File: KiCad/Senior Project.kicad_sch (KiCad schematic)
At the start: 32 parts, among them J1 USB_C_Receptacle_USB2.0_16P, J2 Screw_Terminal_01x02, J3 Screw_Terminal_01x06, SW1 SW_Push, SW2 SW_Push, U1 ESP32-S3FH4R2, X1 FC-135 32.7680KA-A5, Y2 Crystal_GND23

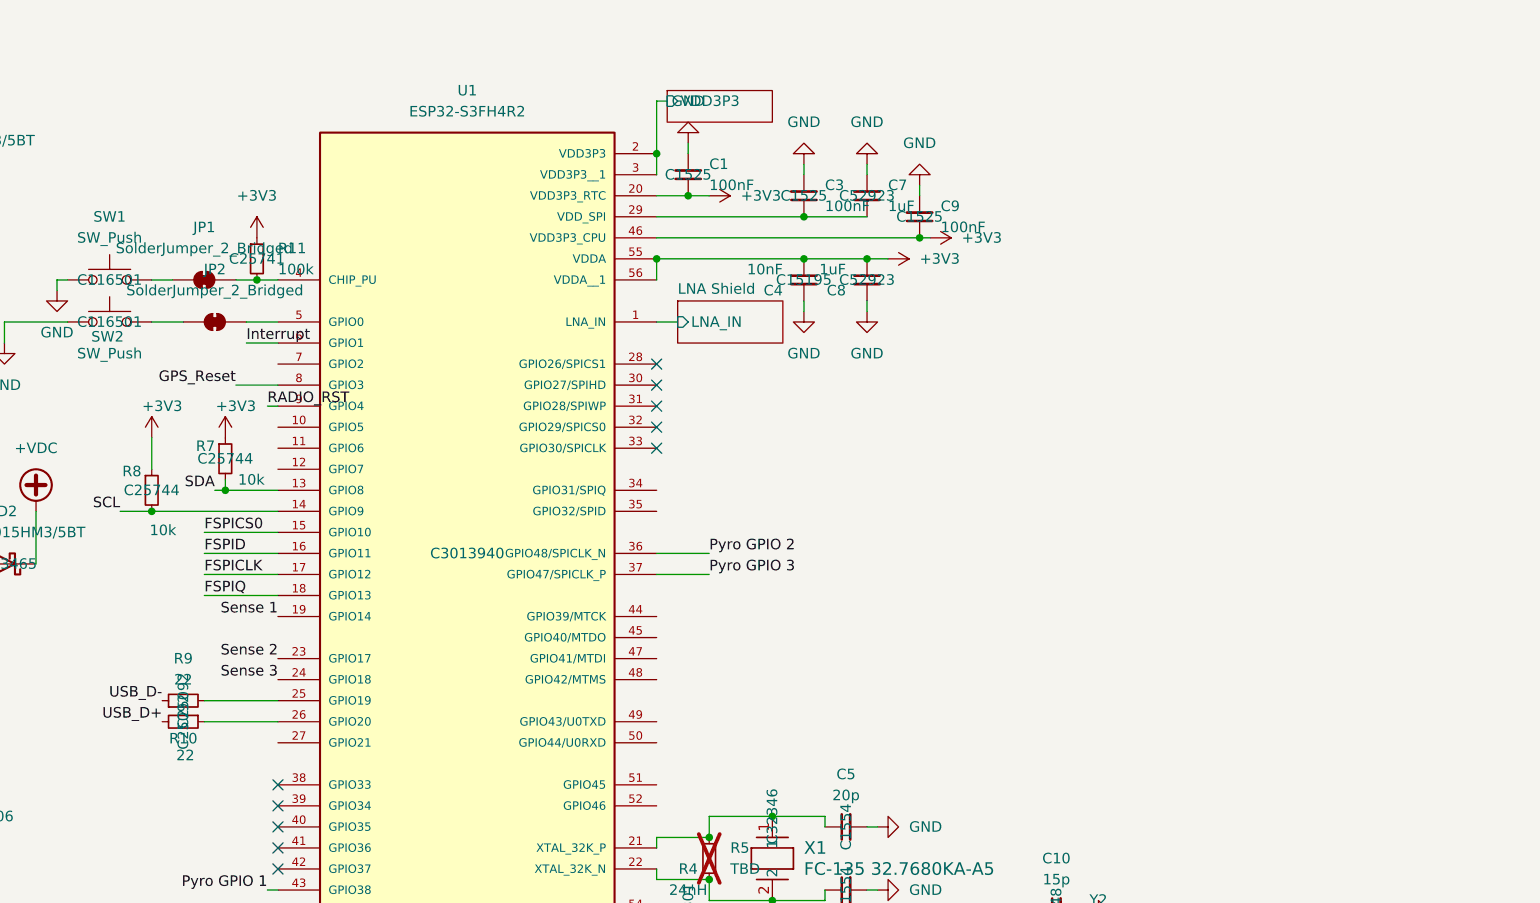
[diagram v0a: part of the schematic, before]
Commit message: adjustments to work with JLC and to match with example
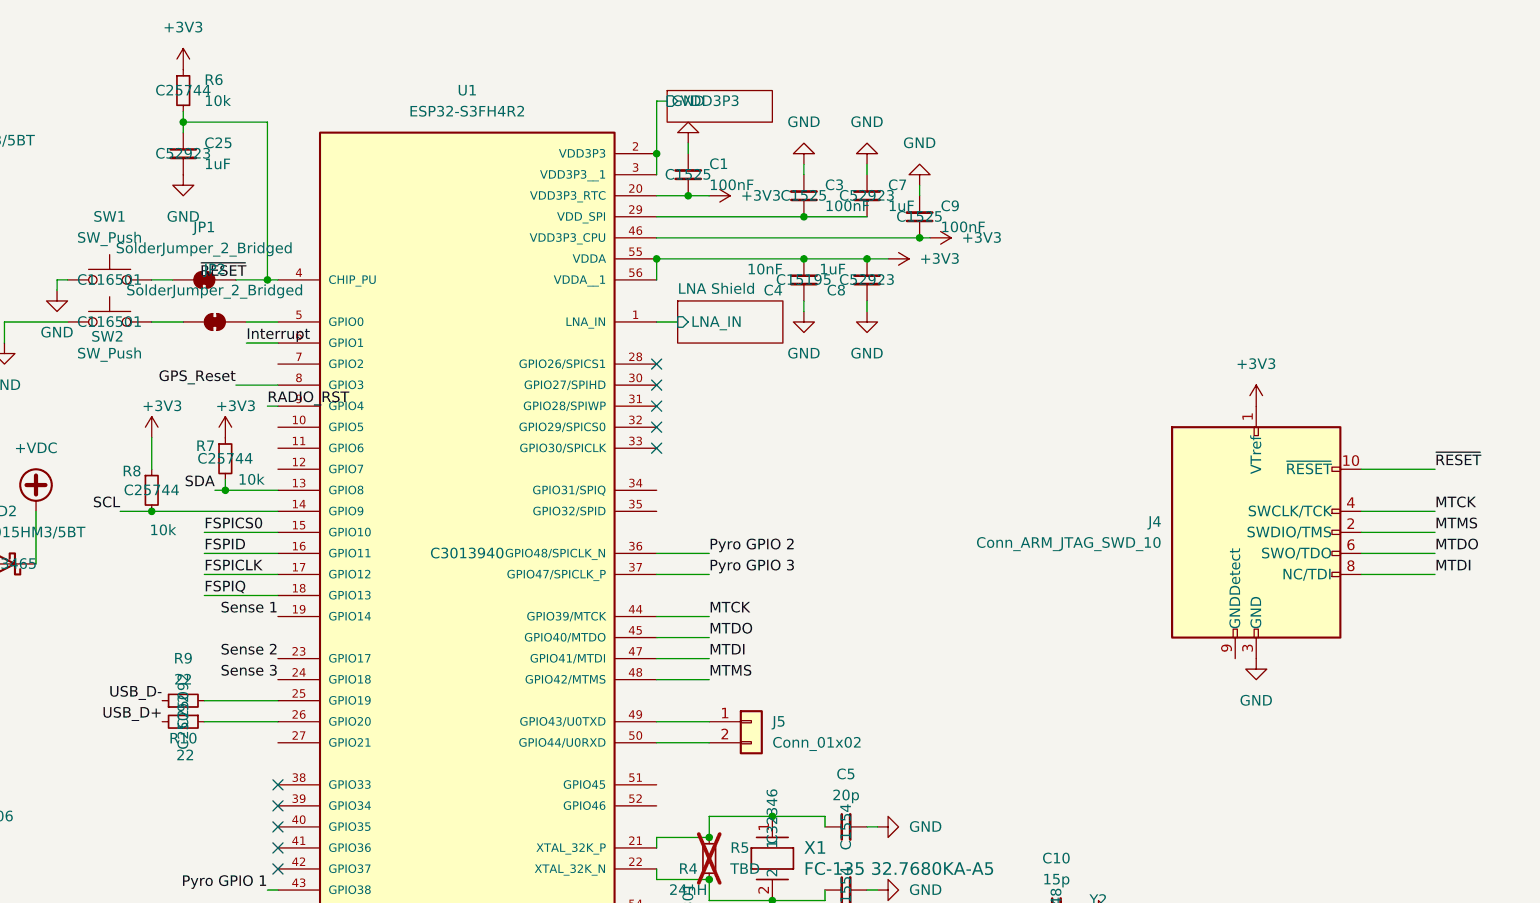
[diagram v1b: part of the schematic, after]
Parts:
- removed R11: 100k, Resistor_SMD:R_0402_1005Metric, symbol Device:R_Small
- added C25: 1uF, Capacitor_SMD:C_0402_1005Metric, symbol Device:C_Small
- added J4: Conn_ARM_JTAG_SWD_10, Connector_PinHeader_1.27mm:PinHeader_2x05_P1.27mm_Vertical_SMD, symbol Connector:Conn_ARM_JTAG_SWD_10
- added J5: Conn_01x02, Connector_PinHeader_1.27mm:PinHeader_1x02_P1.27mm_Vertical_SMD_Pin1Right, symbol Connector_Generic:Conn_01x02
- added R6: 10k, Resistor_SMD:R_0402_1005Metric, symbol Device:R_Small
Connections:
- net +3V3: now also J4.1 (VTref), R6.1
- net GND: now also C25.2, J4.3 (GND), J4.5 (GND)
- net ~{RESET}: now reaches JP1.2 (B), U1.4 (CHIP_PU)
- net ~{RESET}: now also C25.1, J4.10 (~{RESET}), R6.2
- net MTCK: now reaches U1.44 (GPIO39/MTCK)
- net MTCK: now also J4.4 (SWCLK/TCK)
- net MTDO: now reaches U1.45 (GPIO40/MTDO)
- net MTDO: now also J4.6 (SWO/TDO)
- net MTDI: now reaches U1.47 (GPIO41/MTDI)
- net MTDI: now also J4.8 (NC/TDI)
- net MTMS: now reaches U1.48 (GPIO42/MTMS)
- net MTMS: now also J4.2 (SWDIO/TMS)
- net at U1.49 (GPIO43/U0TXD): now also J5.1 (Pin_1)
- net at U1.50 (GPIO44/U0RXD): now also J5.2 (Pin_2)

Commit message: prepare to move barometer to front
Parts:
- J2, J3, J4, J5: now not fitted
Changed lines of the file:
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@@
 		(in_bom yes)
 		(on_board yes)
-		(dnp no)
+		(dnp yes)
 		(fields_autoplaced yes)
 		(property "Reference" "J3"
@@
 		(in_bom yes)
 		(on_board yes)
-		(dnp no)
+		(dnp yes)
 		(fields_autoplaced yes)
 		(property "Reference" "J4"
@@
 		(in_bom yes)
 		(on_board yes)
-		(dnp no)
+		(dnp yes)
 		(fields_autoplaced yes)
 		(property "Reference" "J2"
@@
 		(in_bom yes)
 		(on_board yes)
-		(dnp no)
+		(dnp yes)
 		(fields_autoplaced yes)
 		(property "Reference" "J5"

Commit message: finalize board
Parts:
- added D5: LED, LED_SMD:LED_0603_1608Metric, symbol Device:LED
- added R11: 1, Resistor_SMD:R_2512_6332Metric, symbol Device:R
- added R25: 100k, Resistor_SMD:R_0402_1005Metric, symbol Device:R_Small
- added R27: R_Small, Resistor_SMD:R_0603_1608Metric, symbol Device:R_Small
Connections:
- net +3V3: now also R25.1
- net +BATT: now also R11.1; no longer J3.1 (Pin_1), J3.3 (Pin_3), J3.5 (Pin_5)
- net GND: now also R27.2
- net RADIO_RST: now also R25.2
- net POWER_LED: now reaches U1.10 (GPIO5)
- net POWER_LED: now also D5.2 (A)
- new net: J3.1 (Pin_1), J3.3 (Pin_3), J3.5 (Pin_5), R11.2
- new net: D5.1 (K), R27.1

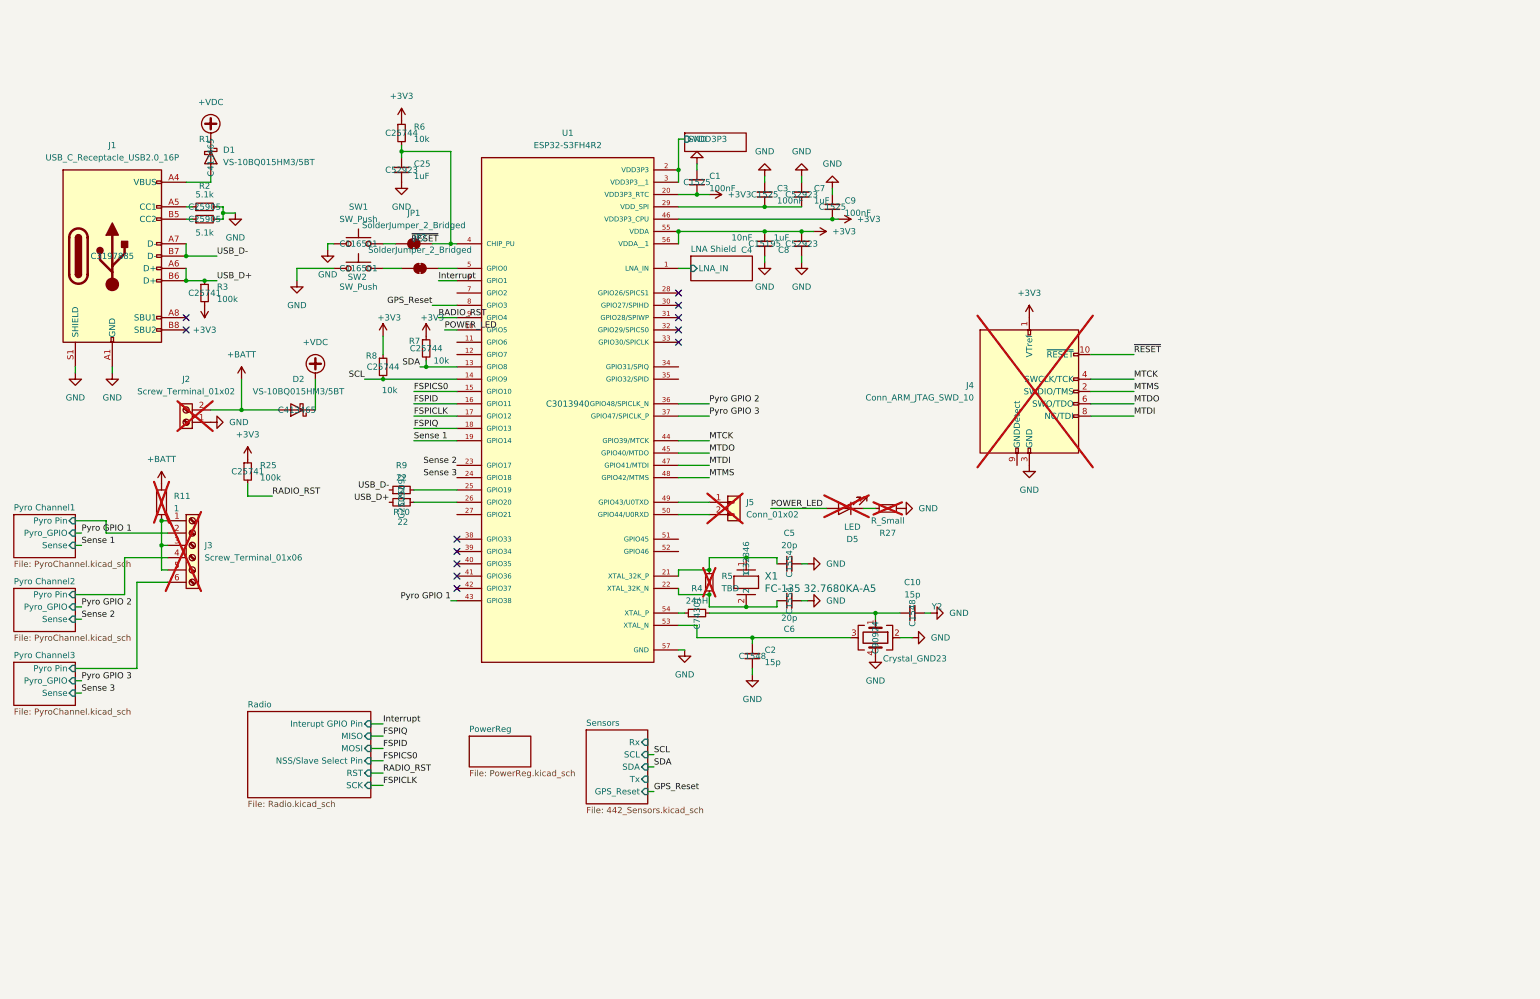
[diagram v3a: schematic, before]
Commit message: clean up schematic, add voltage dividers for measuring battery and charge firing current
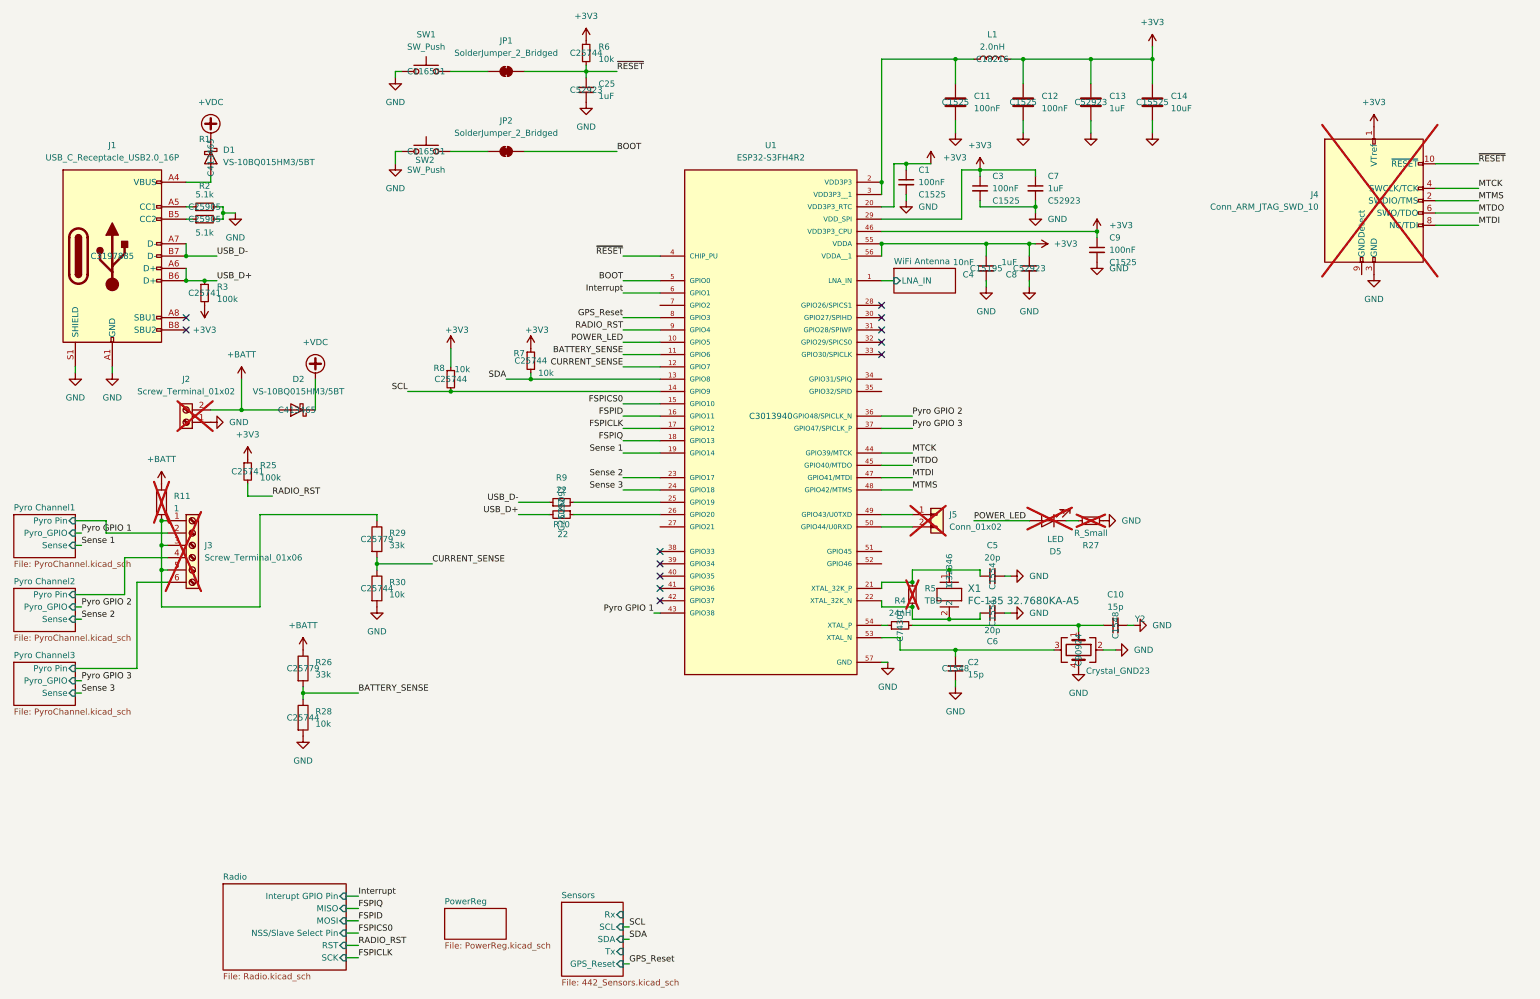
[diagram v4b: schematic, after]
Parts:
- added C11, C12: 100nF, Capacitor_SMD:C_0402_1005Metric, symbol Device:C
- added C13: 1uF, Capacitor_SMD:C_0402_1005Metric, symbol Device:C
- added C14: 10uF, Capacitor_SMD:C_0402_1005Metric, symbol Device:C
- added L1: 2.0nH, Inductor_SMD:L_0402_1005Metric, symbol Device:L
- added R26, R29: 33k, Resistor_SMD:R_0402_1005Metric, symbol Device:R
- added R28, R30: 10k, Resistor_SMD:R_0402_1005Metric, symbol Device:R
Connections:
- net +3V3: now also C3.1, C7.1, U1.29 (VDD_SPI), C12.1, C13.1, C14.1, L1.2
- net +BATT: now also R26.1
- net GND: now also C11.2, C12.2, C13.2, C14.2, R28.2, R30.2
- net BOOT: now reaches JP2.2 (B), U1.5 (GPIO0)
- net BATTERY_SENSE: now reaches U1.11 (GPIO6)
- net BATTERY_SENSE: now also R26.2, R28.1
- net CURRENT_SENSE: now reaches U1.12 (GPIO7)
- net CURRENT_SENSE: now also R29.2, R30.1
- net at J3.1 (Pin_1), J3.3 (Pin_3), J3.5 (Pin_5)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: now also R29.1
- net ESP-32 Power Coupler/VDD3P3: no longer names the net of U1.2 (VDD3P3), U1.3 (VDD3P3__1)
- net ESP-32 Power Coupler/VDD3P3: now also C11.1, L1.1
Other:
- sheet LNA Shield renamed WiFi Antenna
- removed sheet ESP-32 Power Coupler
- moved on the sheet: C1, C10, C2, C25, C3, C4, C5, C6, C7, C8, C9, D5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

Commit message: switch to BMI088 for IMU
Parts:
- J1: LCSC C3197885 -> C2988369
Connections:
- net ~{GYRO_CS}: now reaches U1.27 (GPIO21)
- net ~{ACCELEROMETER_CS}: now reaches U1.7 (GPIO2)
- no-connect marks 12 -> 14
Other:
- sheet Sensors ports: added MISO, MOSI, SCK, ~{ACCELEROMETER_CS}, ~{GYRO_CS}; removed Rx, Tx
- moved on the sheet: R3
